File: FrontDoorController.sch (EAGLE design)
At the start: 9 parts

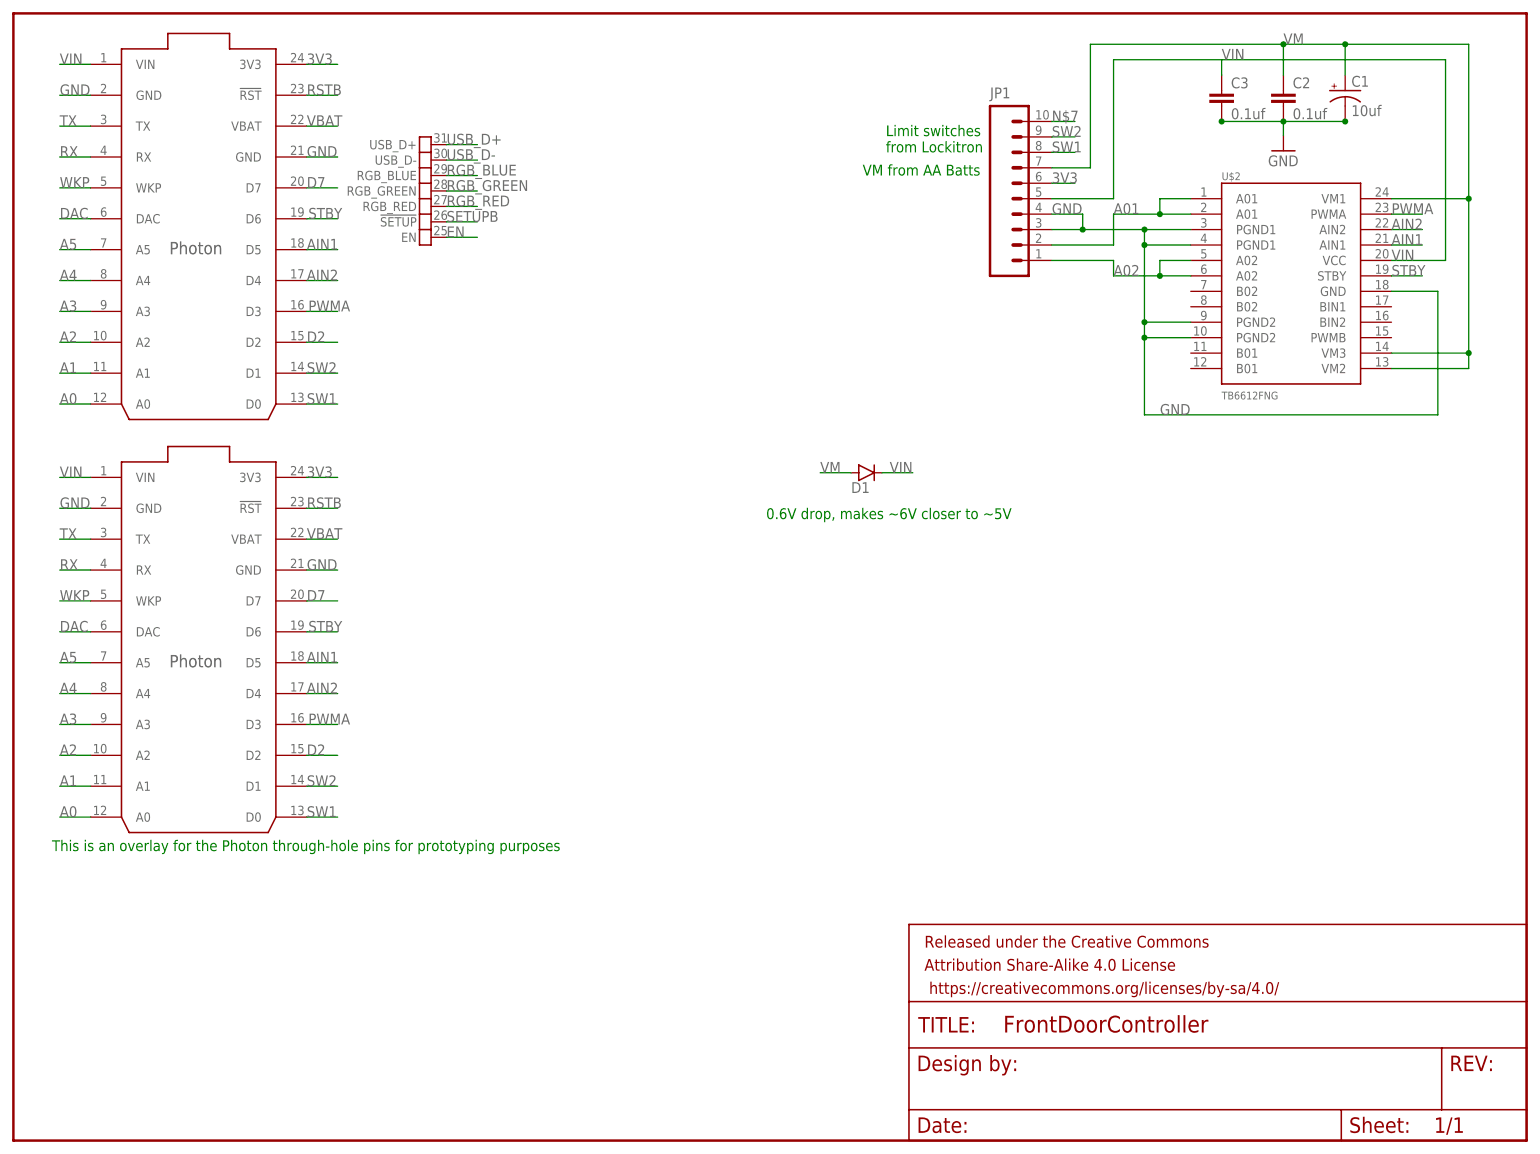
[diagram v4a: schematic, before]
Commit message: Door_Control_PCB: Add reed switch connection
Add a connection point for a reed switch to be used to sense if the door
is open or closed.  Also add a pull down resistor to ensure good
readings and label the pins on the header.
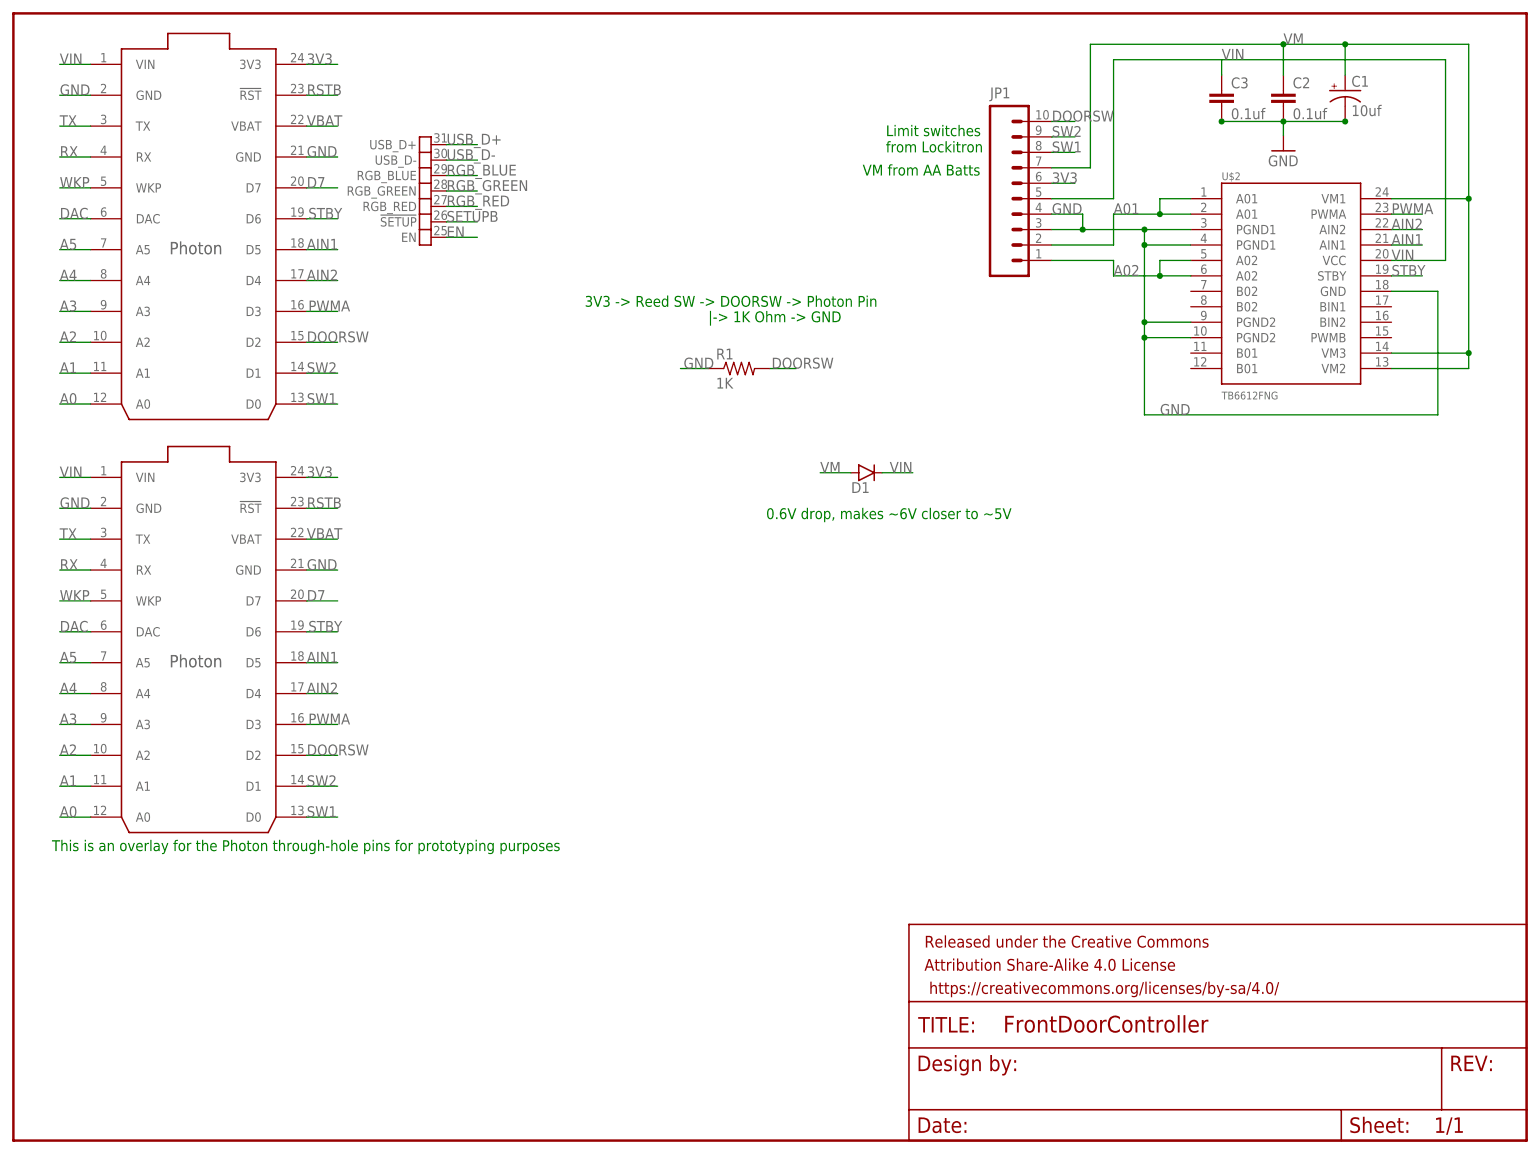
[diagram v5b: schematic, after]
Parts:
- added R1: 1K, SparkFun-Resistors:RESISTOR0603
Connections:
- removed net D2: U$1G$1.D2, U$3.D2
- removed net N$7: JP1.10
- new net DOORSW: JP1.10, R1.2, U$1G$1.D2, U$3.D2
- net GND: now also R1.1
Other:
- note added: "3V3 -> Reed SW -> DOORSW -> Photon Pin"
- note added: "|-> 1K Ohm -> GND"
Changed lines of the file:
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@@
 <setting verticaltext="up"/>
 </settings>
-<grid distance="0.05" unitdist="inch" unit="inch" style="lines" multiple="1" display="no" altdistance="0.025" altunitdist="inch" altunit="inch"/>
+<grid distance="0.1" unitdist="inch" unit="inch" style="lines" multiple="1" display="no" altdistance="0.01" altunitdist="inch" altunit="inch"/>
 <layers>
 <layer number="1" name="Top" color="4" fill="1" visible="no" active="no"/>
@@
 <part name="D1" library="SparkFun-DiscreteSemi" deviceset="DIODE" device="PTH"/>
 <part name="U$3" library="Spark" deviceset="PHOTON" device="_WITH_HEADERS"/>
+<part name="R1" library="SparkFun-Resistors" deviceset="RESISTOR" device="0603" value="1K"/>
 </parts>
 <sheets>
@@
 <text x="143.51" y="162.56" size="1.778" layer="91">Limit switches
 from Lockitron</text>
+<text x="93.98" y="137.16" size="1.778" layer="91">3V3 -&gt; Reed SW -&gt; DOORSW -&gt; Photon Pin</text>
+<text x="114.3" y="134.62" size="1.778" layer="91">|-&gt; 1K Ohm -&gt; GND</text>
 </plain>
 <instances>
@@
 </instance>
 <instance part="U$3" gate="G$1" x="30.48" y="81.153"/>
+<instance part="R1" gate="G$1" x="119.38" y="127"/>
 </instances>
 <busses>
@@
 <label x="48.26" y="93.853" size="1.778" layer="95"/>
 </segment>
+<segment>
+<pinref part="R1" gate="G$1" pin="1"/>
+<wire x1="114.3" y1="127" x2="109.728" y2="127" width="0.1524" layer="91"/>
+<label x="110.236" y="127" size="1.778" layer="95"/>
+</segment>
 </net>
 <net name="TX" class="0">
@@
 <wire x1="48.26" y1="83.693" x2="53.34" y2="83.693" width="0.1524" layer="91"/>
 <label x="48.514" y="83.693" size="1.778" layer="95"/>
-</segment>
-</net>
-<net name="D2" class="0">
-<segment>
-<pinref part="U$1" gate="G$1" pin="D2"/>
-<wire x1="48.26" y1="131.318" x2="53.34" y2="131.318" width="0.1524" layer="91"/>
-<label x="48.26" y="131.318" size="1.778" layer="95"/>
-</segment>
-<segment>
-<pinref part="U$3" gate="G$1" pin="D2"/>
-<wire x1="48.26" y1="63.373" x2="53.34" y2="63.373" width="0.1524" layer="91"/>
-<label x="48.26" y="63.373" size="1.778" layer="95"/>
 </segment>
 </net>
@@
 </segment>
 </net>
-<net name="N$7" class="0">
+<net name="DOORSW" class="0">
 <segment>
 <pinref part="JP1" gate="G$1" pin="10"/>
@@
 <label x="170.815" y="167.64" size="1.778" layer="95"/>
 </segment>
-</net>
+<segment>
+<pinref part="U$1" gate="G$1" pin="D2"/>
+<wire x1="48.26" y1="131.318" x2="53.34" y2="131.318" width="0.1524" layer="91"/>
+<label x="48.26" y="131.318" size="1.778" layer="95"/>
+</segment>
+<segment>
+<pinref part="U$3" gate="G$1" pin="D2"/>
+<wire x1="48.26" y1="63.373" x2="53.34" y2="63.373" width="0.1524" layer="91"/>
+<label x="48.26" y="63.373" size="1.778" layer="95"/>
+</segment>
+<segment>
+<pinref part="R1" gate="G$1" pin="2"/>
+<wire x1="124.46" y1="127" x2="128.778" y2="127" width="0.1524" layer="91"/>
+<label x="124.714" y="127" size="1.778" layer="95"/>
+</segment>
+</net>

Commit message: Door_Control_PCB: Change layer of labels
Change the layer of the header labels because they didn't show up on Osh
Park.
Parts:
- renumbered U$1 to PHOTON
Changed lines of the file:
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@@
 </classes>
 <parts>
-<part name="U$1" library="Spark" deviceset="PHOTON_SMD" device=""/>
+<part name="PHOTON" library="Spark" deviceset="PHOTON_SMD" device=""/>
 <part name="FRAME1" library="SparkFun-Aesthetics" deviceset="FRAME-LETTER" device=""/>
 <part name="U$2" library="SparkFun-PowerIC" deviceset="TB6612FNG" device="" value="TB6612FNG"/>
@@
 </plain>
 <instances>
-<instance part="U$1" gate="G$1" x="30.48" y="149.098"/>
-<instance part="U$1" gate="G$2" x="66.167" y="156.21"/>
+<instance part="PHOTON" gate="G$1" x="30.48" y="149.098"/>
+<instance part="PHOTON" gate="G$2" x="66.167" y="156.21"/>
 <instance part="FRAME1" gate="G$1" x="0" y="0"/>
 <instance part="FRAME1" gate="V" x="147.32" y="0"/>
@@
 <net name="VIN" class="0">
 <segment>
-<pinref part="U$1" gate="G$1" pin="VIN"/>
+<pinref part="PHOTON" gate="G$1" pin="VIN"/>
 <wire x1="12.7" y1="177.038" x2="7.62" y2="177.038" width="0.1524" layer="91"/>
 <label x="7.62" y="177.038" size="1.778" layer="95"/>
@@
 <net name="GND" class="0">
 <segment>
-<pinref part="U$1" gate="G$1" pin="GND@2"/>
+<pinref part="PHOTON" gate="G$1" pin="GND@2"/>
 <wire x1="12.7" y1="171.958" x2="7.62" y2="171.958" width="0.1524" layer="91"/>
 <label x="7.62" y="171.958" size="1.778" layer="95"/>
 </segment>
 <segment>
-<pinref part="U$1" gate="G$1" pin="GND@21"/>
+<pinref part="PHOTON" gate="G$1" pin="GND@21"/>
 <wire x1="48.26" y1="161.798" x2="53.34" y2="161.798" width="0.1524" layer="91"/>
 <label x="48.26" y="161.798" size="1.778" layer="95"/>
@@
 <net name="TX" class="0">
 <segment>
-<pinref part="U$1" gate="G$1" pin="TX"/>
+<pinref part="PHOTON" gate="G$1" pin="TX"/>
 <wire x1="12.7" y1="166.878" x2="7.62" y2="166.878" width="0.1524" layer="91"/>
 <label x="7.62" y="166.878" size="1.778" layer="95"/>
@@
 <net name="RX" class="0">
 <segment>
-<pinref part="U$1" gate="G$1" pin="RX"/>
+<pinref part="PHOTON" gate="G$1" pin="RX"/>
 <wire x1="12.7" y1="161.798" x2="7.62" y2="161.798" width="0.1524" layer="91"/>
 <label x="7.62" y="161.798" size="1.778" layer="95"/>
@@
 <net name="WKP" class="0">
 <segment>
-<pinref part="U$1" gate="G$1" pin="WKP"/>
+<pinref part="PHOTON" gate="G$1" pin="WKP"/>
 <wire x1="12.7" y1="156.718" x2="7.62" y2="156.718" width="0.1524" layer="91"/>
 <label x="7.62" y="156.718" size="1.778" layer="95"/>
@@
 <net name="DAC" class="0">
 <segment>
-<pinref part="U$1" gate="G$1" pin="DAC"/>
+<pinref part="PHOTON" gate="G$1" pin="DAC"/>
 <wire x1="12.7" y1="151.638" x2="7.62" y2="151.638" width="0.1524" layer="91"/>
 <label x="7.62" y="151.638" size="1.778" layer="95"/>
@@
 <net name="A5" class="0">
 <segment>
-<pinref part="U$1" gate="G$1" pin="A5"/>
+<pinref part="PHOTON" gate="G$1" pin="A5"/>
 <wire x1="12.7" y1="146.558" x2="7.62" y2="146.558" width="0.1524" layer="91"/>
 <label x="7.62" y="146.558" size="1.778" layer="95"/>
@@
 <net name="A4" class="0">
 <segment>
-<pinref part="U$1" gate="G$1" pin="A4"/>
+<pinref part="PHOTON" gate="G$1" pin="A4"/>
 <wire x1="12.7" y1="141.478" x2="7.62" y2="141.478" width="0.1524" layer="91"/>
 <label x="7.62" y="141.478" size="1.778" layer="95"/>
@@
 <net name="A3" class="0">
 <segment>
-<pinref part="U$1" gate="G$1" pin="A3"/>
+<pinref part="PHOTON" gate="G$1" pin="A3"/>
 <wire x1="12.7" y1="136.398" x2="7.62" y2="136.398" width="0.1524" layer="91"/>
 <label x="7.62" y="136.398" size="1.778" layer="95"/>
@@
 <net name="A2" class="0">
 <segment>
-<pinref part="U$1" gate="G$1" pin="A2"/>
+<pinref part="PHOTON" gate="G$1" pin="A2"/>
 <wire x1="12.7" y1="131.318" x2="7.62" y2="131.318" width="0.1524" layer="91"/>
 <label x="7.62" y="131.318" size="1.778" layer="95"/>
@@
 <net name="A1" class="0">
 <segment>
-<pinref part="U$1" gate="G$1" pin="A1"/>
+<pinref part="PHOTON" gate="G$1" pin="A1"/>
 <wire x1="12.7" y1="126.238" x2="7.62" y2="126.238" width="0.1524" layer="91"/>
 <label x="7.62" y="126.238" size="1.778" layer="95"/>
@@
 <net name="A0" class="0">
 <segment>
-<pinref part="U$1" gate="G$1" pin="A0"/>
+<pinref part="PHOTON" gate="G$1" pin="A0"/>
 <wire x1="12.7" y1="121.158" x2="7.62" y2="121.158" width="0.1524" layer="91"/>
 <label x="7.62" y="121.158" size="1.778" layer="95"/>
@@
 <net name="3V3" class="0">
 <segment>
-<pinref part="U$1" gate="G$1" pin="3V3"/>
+<pinref part="PHOTON" gate="G$1" pin="3V3"/>
 <wire x1="48.26" y1="177.038" x2="53.34" y2="177.038" width="0.1524" layer="91"/>
 <label x="48.26" y="177.038" size="1.778" layer="95"/>
@@
 <net name="RSTB" class="0">
 <segment>
-<pinref part="U$1" gate="G$1" pin="!RST"/>
+<pinref part="PHOTON" gate="G$1" pin="!RST"/>
 <wire x1="48.26" y1="171.958" x2="53.34" y2="171.958" width="0.1524" layer="91"/>
 <label x="48.26" y="171.958" size="1.778" layer="95"/>
@@
 <net name="D7" class="0">
 <segment>
-<pinref part="U$1" gate="G$1" pin="D7"/>
+<pinref part="PHOTON" gate="G$1" pin="D7"/>
 <wire x1="48.26" y1="156.718" x2="53.34" y2="156.718" width="0.1524" layer="91"/>
 <label x="48.26" y="156.718" size="1.778" layer="95"/>
@@
 <net name="PWMA" class="0">
 <segment>
-<pinref part="U$1" gate="G$1" pin="D3"/>
+<pinref part="PHOTON" gate="G$1" pin="D3"/>
 <wire x1="48.26" y1="136.398" x2="53.34" y2="136.398" width="0.1524" layer="91"/>
 <label x="48.514" y="136.398" size="1.778" layer="95"/>
@@
 <net name="STBY" class="0">
 <segment>
-<pinref part="U$1" gate="G$1" pin="D6"/>
+<pinref part="PHOTON" gate="G$1" pin="D6"/>
 <wire x1="48.26" y1="151.638" x2="53.34" y2="151.638" width="0.1524" layer="91"/>
 <label x="48.514" y="151.638" size="1.778" layer="95"/>
@@
 <net name="USB_D+" class="0">
 <segment>
-<pinref part="U$1" gate="G$2" pin="USB_D+"/>
+<pinref part="PHOTON" gate="G$2" pin="USB_D+"/>
 <wire x1="71.247" y1="163.83" x2="76.327" y2="163.83" width="0.1524" layer="91"/>
 <label x="71.247" y="163.83" size="1.778" layer="95"/>
@@
 <net name="USB_D-" class="0">
 <segment>
-<pinref part="U$1" gate="G$2" pin="USB_D-"/>
+<pinref part="PHOTON" gate="G$2" pin="USB_D-"/>
 <wire x1="71.247" y1="161.29" x2="76.327" y2="161.29" width="0.1524" layer="91"/>
 <label x="71.247" y="161.29" size="1.778" layer="95"/>
@@
 <net name="RGB_BLUE" class="0">
 <segment>
-<pinref part="U$1" gate="G$2" pin="RGB_BLUE"/>
+<pinref part="PHOTON" gate="G$2" pin="RGB_BLUE"/>
 <wire x1="71.247" y1="158.75" x2="76.327" y2="158.75" width="0.1524" layer="91"/>
 <label x="71.247" y="158.75" size="1.778" layer="95"/>
@@
 <net name="RGB_GREEN" class="0">
 <segment>
-<pinref part="U$1" gate="G$2" pin="RGB_GREEN"/>
+<pinref part="PHOTON" gate="G$2" pin="RGB_GREEN"/>
 <wire x1="71.247" y1="156.21" x2="76.327" y2="156.21" width="0.1524" layer="91"/>
 <label x="71.247" y="156.21" size="1.778" layer="95"/>
@@
 <net name="RGB_RED" class="0">
 <segment>
-<pinref part="U$1" gate="G$2" pin="RGB_RED"/>
+<pinref part="PHOTON" gate="G$2" pin="RGB_RED"/>
 <wire x1="71.247" y1="153.67" x2="76.327" y2="153.67" width="0.1524" layer="91"/>
 <label x="71.247" y="153.67" size="1.778" layer="95"/>
@@
 <net name="SETUPB" class="0">
 <segment>
-<pinref part="U$1" gate="G$2" pin="!SETUP"/>
+<pinref part="PHOTON" gate="G$2" pin="!SETUP"/>
 <wire x1="71.247" y1="151.13" x2="76.327" y2="151.13" width="0.1524" layer="91"/>
 <label x="71.247" y="151.13" size="1.778" layer="95"/>
@@
 <net name="EN" class="0">
 <segment>
-<pinref part="U$1" gate="G$2" pin="EN"/>
+<pinref part="PHOTON" gate="G$2" pin="EN"/>
 <wire x1="71.247" y1="148.59" x2="76.327" y2="148.59" width="0.1524" layer="91"/>
 <label x="71.247" y="148.59" size="1.778" layer="95"/>
@@
 </segment>
 <segment>
-<pinref part="U$1" gate="G$1" pin="D5"/>
+<pinref part="PHOTON" gate="G$1" pin="D5"/>
 <wire x1="48.26" y1="146.558" x2="53.34" y2="146.558" width="0.1524" layer="91"/>
 <label x="48.26" y="146.558" size="1.778" layer="95"/>
@@
 </segment>
 <segment>
-<pinref part="U$1" gate="G$1" pin="D4"/>
+<pinref part="PHOTON" gate="G$1" pin="D4"/>
 <wire x1="48.26" y1="141.478" x2="53.34" y2="141.478" width="0.1524" layer="91"/>
 <label x="48.26" y="141.478" size="1.778" layer="95"/>
@@
 <net name="VBAT" class="0">
 <segment>
-<pinref part="U$1" gate="G$1" pin="VBAT"/>
+<pinref part="PHOTON" gate="G$1" pin="VBAT"/>
 <wire x1="48.26" y1="166.878" x2="53.34" y2="166.878" width="0.1524" layer="91"/>
 <label x="48.26" y="166.878" size="1.778" layer="95"/>
@@
 </segment>
 <segment>
-<pinref part="U$1" gate="G$1" pin="D0"/>
+<pinref part="PHOTON" gate="G$1" pin="D0"/>
 <wire x1="48.26" y1="121.158" x2="53.34" y2="121.158" width="0.1524" layer="91"/>
 <label x="48.26" y="121.158" size="1.778" layer="95"/>
@@
 </segment>
 <segment>
-<pinref part="U$1" gate="G$1" pin="D1"/>
+<pinref part="PHOTON" gate="G$1" pin="D1"/>
 <wire x1="48.26" y1="126.238" x2="53.34" y2="126.238" width="0.1524" layer="91"/>
 <label x="48.26" y="126.238" size="1.778" layer="95"/>
@@
 </segment>
 <segment>
-<pinref part="U$1" gate="G$1" pin="D2"/>
+<pinref part="PHOTON" gate="G$1" pin="D2"/>
 <wire x1="48.26" y1="131.318" x2="53.34" y2="131.318" width="0.1524" layer="91"/>
 <label x="48.26" y="131.318" size="1.778" layer="95"/>
